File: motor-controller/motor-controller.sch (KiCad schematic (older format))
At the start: 19 parts, among them J1 Molex 172043-0201 R/A, J2 Molex 172043-0302 R/A, J3 MCU-IO, U1 DRV10983PWP

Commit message: Added isolation for digital signals going offboard to schematic.
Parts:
- removed R3: 4.7k, Resistor_SMD:R_0603_1608Metric, symbol Device:R_Small
- added C?: C, symbol Device:C
- added R? (x4): 4.7k, Resistor_SMD:R_0603_1608Metric, symbol Device:R_Small
- added R? (x2): 75, symbol Device:R
- added R? (x3): R, symbol Device:R
- added U? (x3): TLP291-4, Package_SO:SOIC-16_4.55x10.3mm_P1.27mm, symbol Isolator:TLP291-4
- added U?: SI8600AC, Package_SO:SOIC-8_3.9x4.9mm_P1.27mm, symbol custom:SI8600AC
- J3: footprint Connector_JST:JST_XH_B05B-XH-AM_1x05_P2.50mm_Vertical -> Connector_JST:JST_XH_B07B-XH-AM_1x07_P2.50mm_Vertical; symbol Connector:Conn_01x05_Male -> Connector:Conn_01x07_Male
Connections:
- net +3V3: now also R?.1, R?.1, U?.14, U?.16, U?.5, U?.8 (VDDB)
- net GND: now also R?.2, R?.2, U?.5 (GNDB)
- net SDA-MTR: now reaches R1.2, U1.10 (SCL)
- net SDA-MTR: now also R?.2, U?.7 (BSDA); no longer J3.1 (Pin_1)
- net SCL-MTR: now reaches R2.2, U1.11 (SDA)
- net SCL-MTR: now also R?.2, U?.6 (BSCL); no longer J3.2 (Pin_2)
- net FG-MTR: now reaches U1.12 (FG)
- net FG-MTR: now also U?.6; no longer J3.3 (Pin_3)
- net DIR renamed DIR-MTR
- net DIR-MTR: now also R?.1, U?.15; no longer J3.4 (Pin_4)
- net SPEED renamed SPEED-MTR
- net SPEED-MTR: now also R?.1, U?.13; no longer J3.5 (Pin_5)
- new net +5V: C?.1, J3.6 (Pin_6), R?.1, R?.1, U?.1 (VDDA), U?.12
- new net DIR-uC: J3.4 (Pin_4), R?.1, U?.2
- new net FG-uC: J3.3 (Pin_3), R?.1, U?.11
- new net GNDD: C?.2, J3.7 (Pin_7), R?.2, R?.2, R?.2, U?.4 (GNDA)
- new net IN: U?.1, U?.3
- new net SCL-uC: J3.1 (Pin_1), R?.2, U?.3 (ASCL)
- new net SDA-uC: J3.2 (Pin_2), R?.2, U?.2 (ASDA)
- new net SPEED-uC: J3.5 (Pin_5), R?.1, U?.4
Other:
- note added: "======== Bidirectional I2C isolation ========"
- note added: "======== Unidirectional signal isolation ========"
- note added: "Decoupling, uC-side power.\nPlace close to I2C isolator."
- note added: "LEDs in optoisolators drop approx. 1.4V \nat full current of 50 mA. For 5V inputs, \nthis requires a 72 Ohm resistor to keep\nthe current below the 50 mA maximum.\nFor 3.3V inputs, a 38 Ohm resistor will \nkeep LED the current below the maximum.\n\n75 and 39 Ohm resistors selected b/c they \nare more common.\n\nFG-MTR is the motor controller odometry \noutput. It is an open drain output that can 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"
- moved on the sheet: C1, C2, C3, C4, C5, C6, F1, H1, H2, H3, H4, J1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

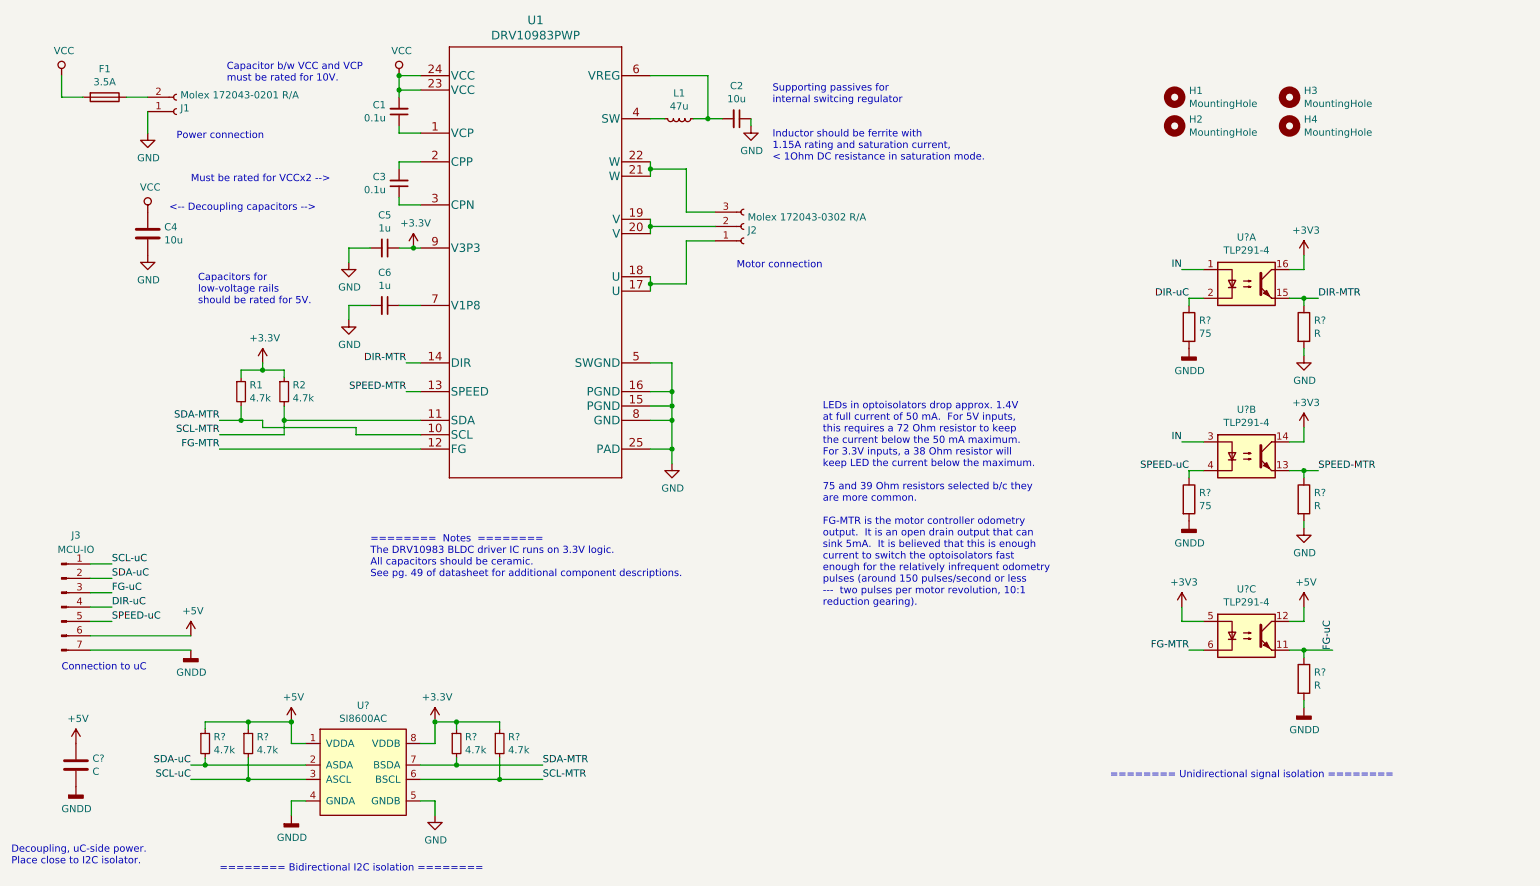
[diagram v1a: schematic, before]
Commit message: Optoisolation modifications and pre-layout changes.
Added NPN to optoisolator output of PWM input signal for faster switching.
Set resistor values on optoisolator output for non-open-collector signals
to 200 ohms.  Added back pullup resistor to odometry output just in case;
the footprint should remain unpopulated unless there is a misunderstanding
for how the odometry output works.
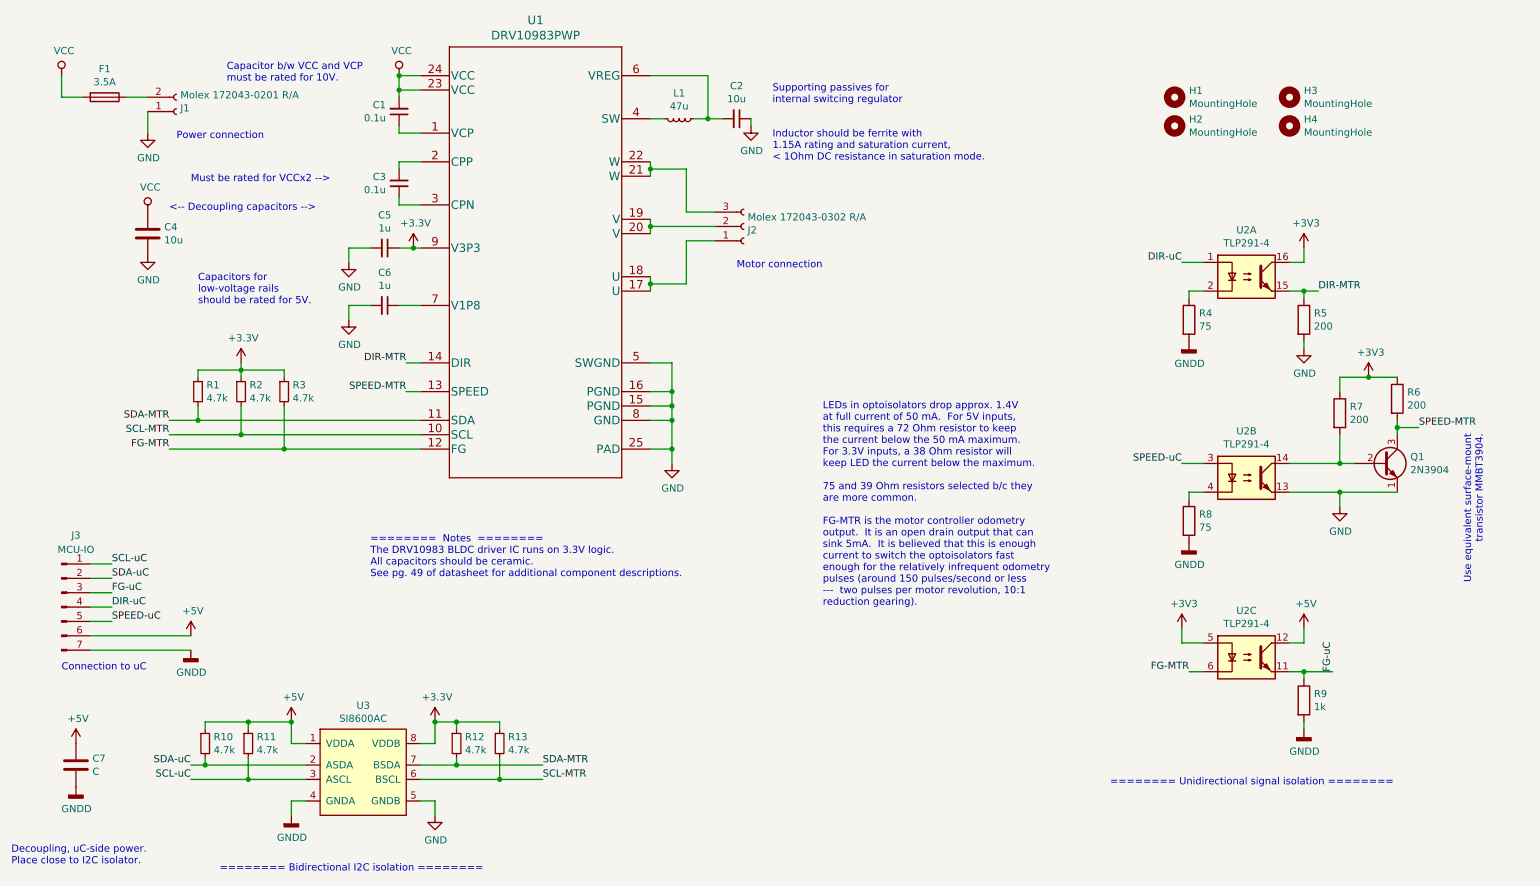
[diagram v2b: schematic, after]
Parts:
- added Q1: 2N3904, Package_TO_SOT_SMD:SOT-23, symbol Transistor_BJT:2N3904
- added R3: 4.7k, Resistor_SMD:R_0603_1608Metric, symbol Device:R_Small
- added R6: 200, Resistor_SMD:R_0603_1608Metric, symbol Device:R
- C7: renamed from C?; footprint (none) -> Capacitor_SMD:C_0603_1608Metric
- R4, R8: renamed from R?; footprint (none) -> Resistor_SMD:R_0603_1608Metric
- R5, R7: renamed from R?; value R -> 200; footprint (none) -> Resistor_SMD:R_0603_1608Metric
- R9: renamed from R?; value R -> 1k; footprint (none) -> Resistor_SMD:R_0603_1608Metric
- gave numbers to parts that had none: 6
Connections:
- net +3V3: now also R7.1, R3.1, R6.1; no longer U2.14
- net DIR-uC: now also U2.1; no longer R4.1, U2.2
- net FG-MTR: now also R3.2
- net GND: now also U2.13, Q1.1 (E); no longer R7.2
- net SCL-MTR: now also U1.10 (SCL); no longer U1.11 (SDA)
- net SDA-MTR: now also U1.11 (SDA); no longer U1.10 (SCL)
- net SPEED-MTR: now also Q1.3 (C), R6.2; no longer R7.1, U2.13
- net SPEED-uC: now also U2.3; no longer R8.1, U2.4
- removed net IN: U2.1, U2.3
- new net: R4.1, U2.2
- new net: Q1.2 (B), R7.2, U2.14
- new net: R8.1, U2.4
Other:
- note added: "Use equivalent surface-mount \ntransistor MMBT3904."
- moved on the sheet: R1, R2, R4, R5, R7, R8, R9, U2A, U2B, U2C

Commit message: Prelayout modifications; changed 7-pin connector pinout to permit tighter layout.
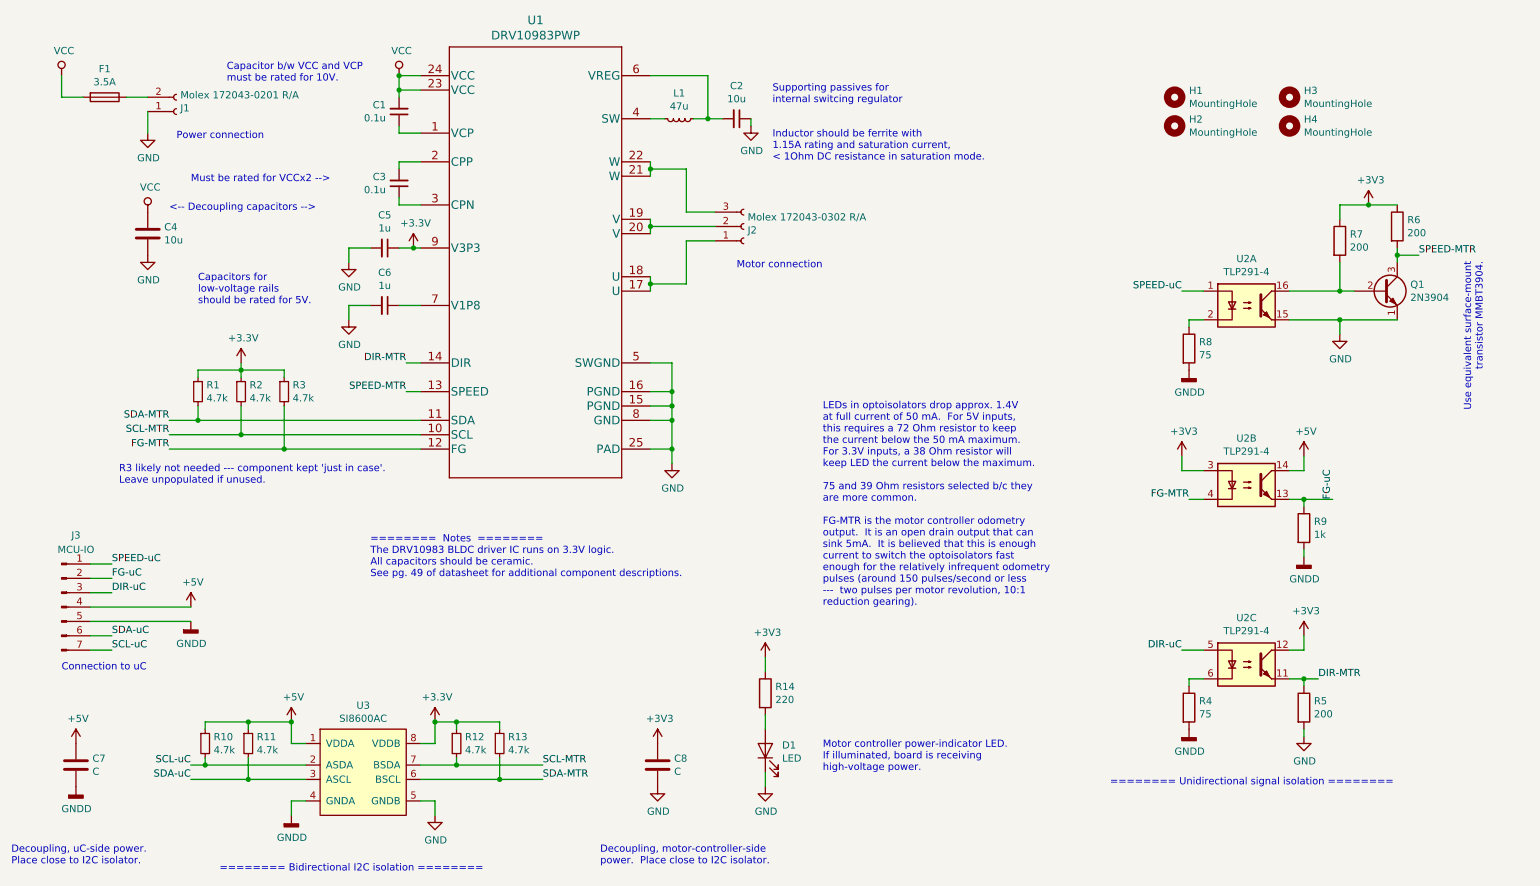
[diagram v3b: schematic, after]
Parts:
- added C8: C, Capacitor_SMD:C_0201_0603Metric, symbol Device:C
- added D1: LED, LED_SMD:LED_0603_1608Metric, symbol Device:LED
- added R14: 220, Resistor_SMD:R_0603_1608Metric, symbol Device:R
- J3: footprint Connector_JST:JST_XH_B07B-XH-AM_1x07_P2.50mm_Vertical -> Connector_JST:JST_XH_B07B-XH-A_1x07_P2.50mm_Vertical
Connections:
- net +3V3: now also U2.12, U2.3, C8.1, R14.1; no longer U2.16, U2.5
- net +5V: now also J3.4 (Pin_4), U2.14; no longer J3.6 (Pin_6), U2.12
- net DIR-MTR: now also U2.11; no longer U2.15
- net DIR-uC: now also J3.3 (Pin_3), U2.5; no longer J3.4 (Pin_4), U2.1
- net FG-MTR: now also U2.4; no longer U2.6
- net FG-uC: now also J3.2 (Pin_2), U2.13; no longer J3.3 (Pin_3), U2.11
- net GND: now also U2.15, C8.2, D1.1 (K); no longer U2.13
- net GNDD: now also J3.5 (Pin_5); no longer J3.7 (Pin_7)
- net SCL-MTR: now also R12.2, U3.7 (BSDA); no longer R13.2, U3.6 (BSCL)
- net SCL-uC: now also J3.7 (Pin_7), R10.2, U3.2 (ASDA); no longer J3.1 (Pin_1), R11.2, U3.3 (ASCL)
- net SDA-MTR: now also R13.2, U3.6 (BSCL); no longer R12.2, U3.7 (BSDA)
- net SDA-uC: now also J3.6 (Pin_6), R11.2, U3.3 (ASCL); no longer J3.2 (Pin_2), R10.2, U3.2 (ASDA)
- net SPEED-uC: now also J3.1 (Pin_1), U2.1; no longer J3.5 (Pin_5), U2.3
- net at U2.2: now also R8.1; no longer R4.1
- net at Q1.2 (B), R7.2: now also U2.16; no longer U2.14
- new net: R4.1, U2.6
- new net: D1.2 (A), R14.2
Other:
- note added: "Decoupling, motor-controller-side \npower. Place close to I2C isolator."
- note added: "Motor controller power-indicator LED.\nIf illuminated, board is receiving \nhigh-voltage power."
- note added: "R3 likely not needed --- component kept 'just in case'.\nLeave unpopulated if unused."
- moved on the sheet: Q1, R4, R5, R6, R7, R8, R9, U2A, U2B, U2C
